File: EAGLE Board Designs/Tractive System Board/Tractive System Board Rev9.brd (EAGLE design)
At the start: 200 x 65 mm, 151 parts, among them K1 RELAY_SPST_NO_D_24, Q2 TRANSISTOR_N_MOS__PMV15ENEA, U1 OPAMP_1_CHANNEL_OPA991, U10 LTC6994-2, U5 RELAY_SOLIDSTATE_NO_AB38S-Q-A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, U6 LT8315, U7 AMC3330_AIRGAP, U8 AMC3330_AIRGAP

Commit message: update
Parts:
- moved D9 61.6 mm to (86.2, 27.4)
- moved D2 46.0 mm to (87.7, 23.3), turned to 270 degrees
- moved R15 45.5 mm to (86.1, 23.5), turned to 90 degrees
- moved R40 44.3 mm to (84.0, 22.8), turned to 270 degrees
- moved R49 43.7 mm to (82.5, 22.8), turned to 90 degrees
- moved C30 43.5 mm to (80.9, 22.7), turned to 270 degrees
- moved R51 42.9 mm to (78.7, 22.1), turned to 0 degrees
- moved D12 42.3 mm to (47.8, 13.2), turned to 90 degrees
- moved C9 40.9 mm to (52.3, 13.4), turned to 270 degrees
- moved C6 40.9 mm to (50.7, 13.4), turned to 270 degrees
- moved R18 40.6 mm to (87.6, 19.8), turned to 90 degrees
- moved C56 40.0 mm to (86.1, 19.7), turned to 270 degrees
- moved L1 39.7 mm to (66.7, 17.0), turned to 180 degrees
- moved C5 39.1 mm to (54.5, 14.3), turned to 270 degrees
- moved C3 38.1 mm to (57.1, 14.2), turned to 270 degrees
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
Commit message: update
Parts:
- moved D12 44.2 mm to (26.2, -25.4), turned to 180 degrees
- moved R15 43.7 mm to (52.4, -4.36), turned to 180 degrees
- moved R40 43.1 mm to (52.1, -6.19), turned to 0 degrees
- moved R49 43.0 mm to (52.1, -7.71), turned to 180 degrees
- moved C30 42.9 mm to (52.2, -9.23), turned to 0 degrees
- moved R51 42.8 mm to (52.8, -12.0), turned to 90 degrees
- moved C3 41.8 mm to (34.3, -20.8)
- moved C5 41.8 mm to (31.6, -20.8)
- moved L1 41.8 mm to (43.8, -18.0)
- moved D2 40.6 mm to (62.9, -8.84), turned to 180 degrees
- moved C6 40.6 mm to (27.9, -20.1)
- moved C9 40.6 mm to (29.5, -20.1)
- moved D11 39.9 mm to (54.5, -16.6), turned to 180 degrees
- moved R18 39.4 mm to (55.9, -3.56), turned to 180 degrees
- moved TS-FUSED 39.0 mm to (69.1, -23.6)
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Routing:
- net TS+FUSED: track 142.7 -> 131.4 mm
- net TS-FUSED: vias 13 -> 12

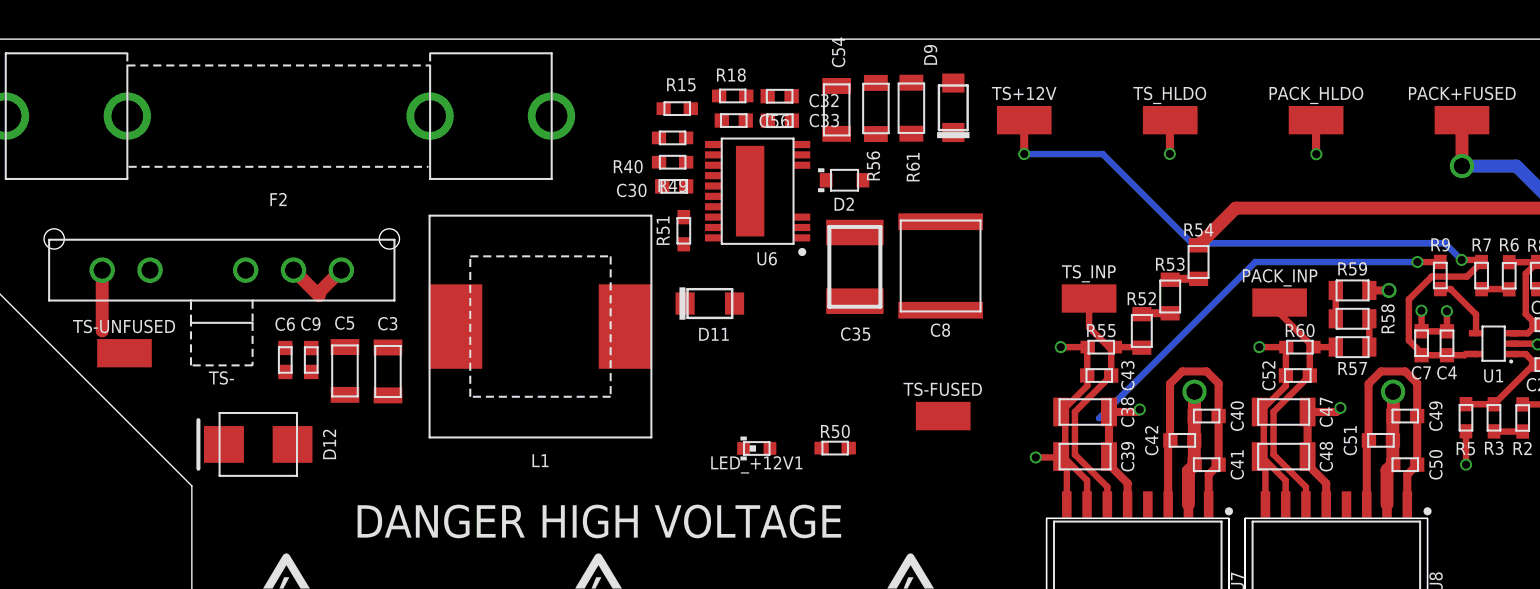
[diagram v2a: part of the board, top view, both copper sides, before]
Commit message: rev9-reroute-first-attempt
modified based on femke's design
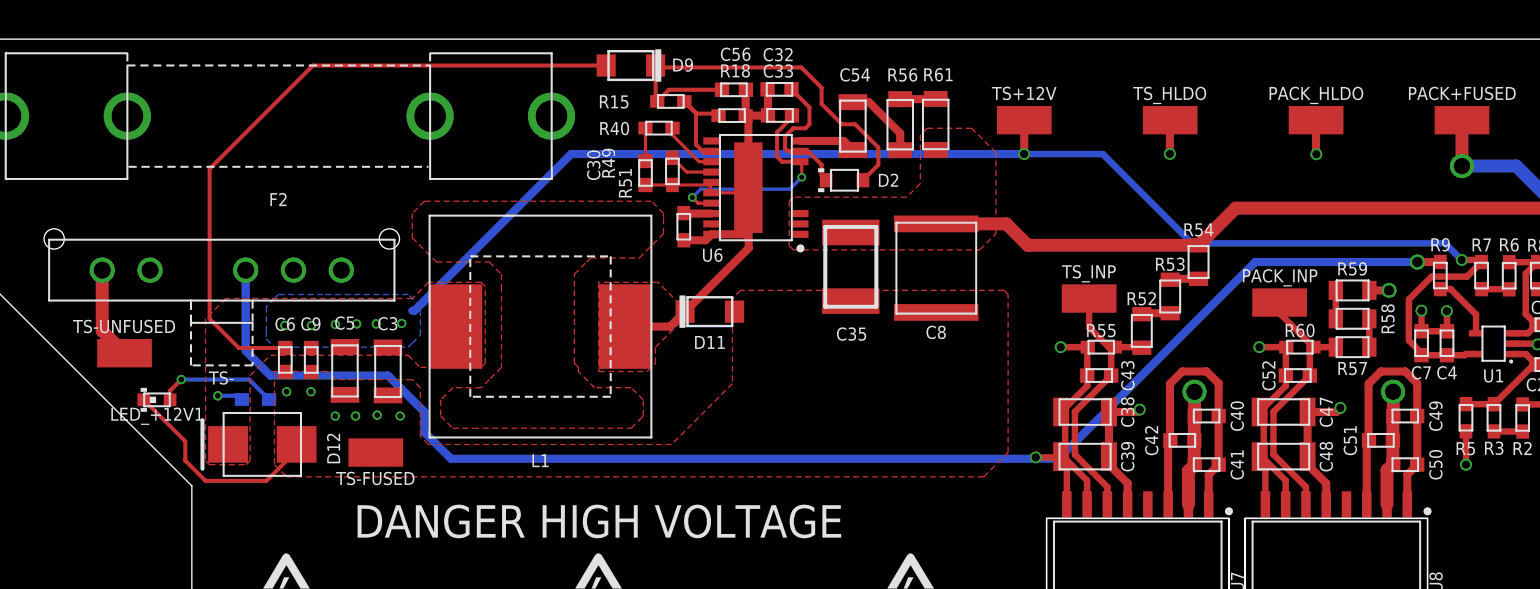
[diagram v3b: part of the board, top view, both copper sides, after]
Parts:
- moved LED_+12V1 37.7 mm to (19.8, -22.6)
- moved R50 36.4 mm to (26.0, -22.6), flipped to the bottom
- moved TS-FUSED 35.6 mm to (33.5, -25.9)
- moved D9 20.4 mm to (49.5, -1.65), turned to 0 degrees
- moved C30 1.99 mm to (50.4, -8.39), turned to 270 degrees
- moved C56 1.93 mm to (56.0, -3.17)
- moved R56 1.83 mm to (66.4, -5.36)
- moved R61 1.83 mm to (68.6, -5.35)
- moved C54 1.44 mm to (63.4, -5.45)
- moved R18 1.23 mm to (55.9, -4.79)
- moved R40 1.05 mm to (51.3, -5.58)
- moved R15 0.60 mm to (52.0, -3.91)
- moved R49 0.57 mm to (52.1, -8.29), turned to 90 degrees
- moved D11 0.51 mm to (54.5, -17.1)
- moved C32 0.43 mm to (58.8, -3.15)
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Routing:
- net TS+12V: track 46.5 -> 132.9 mm, vias 2 -> 9
- net AIL+: track 26.0 -> 88.6 mm
- net PGND: track 0.00 -> 38.4 mm
- net N$1: track 0.00 -> 25.8 mm
- net TS+FUSED: track 131.4 -> 148.4 mm
- net INTVCC: track 0.00 -> 14.3 mm, vias 0 -> 2
- net TS-FUSED: track 65.0 -> 74.1 mm, vias 12 -> 18
- net BIAS: track 0.00 -> 9.05 mm
- net N$44: track 0.00 -> 7.58 mm, vias 0 -> 1
- net FB: track 0.00 -> 6.66 mm
- net N$35: track 0.00 -> 4.84 mm
- net VC: track 0.00 -> 3.58 mm
- net DCM: track 0.00 -> 3.54 mm
- net IREG/SS: track 0.00 -> 2.82 mm
- net N$34: track 0.00 -> 2.23 mm
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- added copper zone on layer 1, net CUTOUT
- added copper zone on layer 1, net PGND
- added copper zone on layer 1, net TS+12V
- added copper zone on layer 16, net TS+12V
- added copper zone on layer 1, net TS+FUSED
- added copper zone on layer 1, net TS-FUSED

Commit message: small update
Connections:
- net PGND renamed SW
- net PACK+FUSED: no longer R4.2
- net TS+FUSED: now also R4.2
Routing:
- net TS+12V: track 132.9 -> 162.3 mm
- net TS+FUSED: track 148.4 -> 164.8 mm
- net AIL+: track 88.6 -> 80.3 mm
- net PACK+FUSED: track 41.7 -> 37.4 mm, vias 3 -> 2
- net SW: track 38.4 -> 34.4 mm
- net N$1: track 25.8 -> 23.3 mm
- net TS-FUSED: vias 18 -> 37

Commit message: updated precharge relay
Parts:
- K1: value RELAY_SPST_NO_D_24 -> RELAY_SPST_NO_D_200W_24
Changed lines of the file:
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@@
 <drawing>
 <settings>
-<setting alwaysvectorfont="no"/>
+<setting alwaysvectorfont="yes"/>
 <setting keepoldvectorfont="yes"/>
 <setting verticaltext="up"/>
@@
 <attribute name="NAME" x="44.704" y="-50.546" size="1.27" layer="25" font="vector" rot="R270" align="bottom-center"/>
 </element>
-<element name="K1" library="HyTechDevices" package="D" value="RELAY_SPST_NO_D_24" x="138.938" y="-46.99" smashed="yes" rot="R180">
-<attribute name="DKPN" value="725-1048-ND" x="95.758" y="-5.08" size="1.778" layer="27" rot="R180" display="off"/>
+<element name="K1" library="HyTechDevices" package="D" value="RELAY_SPST_NO_D_200W_24" x="138.938" y="-46.99" smashed="yes" rot="R180">
+<attribute name="DKPN" value="725-1362-ND" x="95.758" y="-5.08" size="1.778" layer="27" rot="R180" display="off"/>
 <attribute name="MANUFACTURER" value="Sensata-Cynergy3" x="95.758" y="-5.08" size="1.778" layer="27" rot="R180" display="off"/>
-<attribute name="MOPN" value="285-DAR72410" x="95.758" y="-5.08" size="1.778" layer="27" rot="R180" display="off"/>
-<attribute name="MPN" value="DAR72410" x="95.758" y="-5.08" size="1.778" layer="27" rot="R180" display="off"/>
+<attribute name="MOPN" value="285-DAT200-24" x="95.758" y="-5.08" size="1.778" layer="27" rot="R180" display="off"/>
+<attribute name="MPN" value="DAT200-24" x="95.758" y="-5.08" size="1.778" layer="27" rot="R180" display="off"/>
 <attribute name="NAME" x="169.9" y="-47.018" size="0.8128" layer="21" font="vector" rot="R270" align="bottom-center"/>
 </element>
@@
 <vertex x="55.88" y="-21.59"/>
 <vertex x="52.07" y="-25.4"/>
-<vertex x="36.83" y="-25.4"/>
-<vertex x="36.322" y="-24.892"/>
+<vertex x="36.576" y="-25.4"/>
+<vertex x="36.322" y="-25.146"/>
 <vertex x="36.322" y="-21.844"/>
 <vertex x="35.814" y="-21.336"/>

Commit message: sch changes from testing
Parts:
- removed C56: CAPACITOR_0603_50V_10NF, HyTechDevices:0603-CAP
- removed R49: RESISTOR_0603_5.9K, HyTechDevices:0603-RES
- added C10: CAPACITOR_0603_50V_0.1UF, HyTechDevices:0603-CAP
- added D1: RECTIFIER_800V_SOD-123FA, HyTechDevices:SOD-123FA
- added R1: RESISTOR_0603_DNP, HyTechDevices:0603-RES
- R30: value RESISTOR_0603_3.3K -> RESISTOR_0603_12K
- R42: value RESISTOR_0603_DNP -> RESISTOR_0603_12K
- moved TS+12V 5.08 mm to (79.2, -5.08)
- moved TS_HLDO 3.56 mm to (86.9, -5.08)
- moved PACK_HLDO 2.54 mm to (95.0, -5.08)
- moved PACK+FUSED 1.27 mm to (102.9, -5.08)
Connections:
- new net DRAIN: C35.1, C8.1, D1.C, R61.1, U6.1, U6.2, U6.3
- new net N$4: R1.2
- net IREG/SS: now also C10.1; no longer R49.2
- net N$1: no longer C56.1
- net SW: now also C10.2; no longer C56.2, R49.1
- net TS+12V: now also R1.1
- net TS+FUSED: now also D1.A; no longer C35.1, C8.1, R54.2, R61.1, U6.1, U6.2, U6.3
- net TS+UNFUSED: now also R54.2
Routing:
- net TS+FUSED: track 164.8 -> 156.0 mm
- net SW: track 34.4 -> 30.5 mm
- net TS_HLDO_OUT: track 27.2 -> 28.7 mm
- net N$1: track 23.3 -> 21.9 mm
- net IREG/SS: track 2.82 -> 1.56 mm
- net PACK+FUSED: track 37.4 -> 36.3 mm

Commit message: some more routing
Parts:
- added J1: CONNECTOR-2_μF_T_V_BLACK, HyTechDevices:MOLEX_MICROFIT_PTH_VERTICAL_02_DUAL
- moved D1 97.4 mm to (76.2, -10.7), turned to 180 degrees
- moved C10 85.2 mm to (52.1, -8.38), turned to 270 degrees
- moved R1 67.5 mm to (26.4, -7.62), flipped to the bottom, turned to 180 degrees
- moved TS+ 6.37 mm to (191.0, -42.9)
- moved R54 2.90 mm to (82.3, -14.7), turned to 0 degrees
- moved R53 1.13 mm to (82.3, -16.6), turned to 180 degrees
- moved R52 0.80 mm to (82.3, -18.5), turned to 0 degrees
- moved R9 0.77 mm to (100.2, -15.6), flipped to the bottom, turned to 180 degrees
- moved R4 0.25 mm to (107.3, -24.0)
- turned R5 to 270 degrees
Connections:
- removed net N$4: R1.2
- net AIL+: now also J1.1, R1.2
- net TS-FUSED: now also J1.2
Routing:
- net AIL+: track 80.3 -> 271.5 mm, vias 1 -> 0
- net TS-FUSED: track 74.1 -> 193.3 mm, vias 37 -> 38
- net TS+UNFUSED: track 103.5 -> 149.2 mm, vias 0 -> 1
- net IT-: track 72.0 -> 52.7 mm
- net IT+: track 73.1 -> 53.8 mm
- net TS+FUSED: track 156.0 -> 163.5 mm
- net DRAIN: track 0.00 -> 6.37 mm
- net PACK+: track 133.9 -> 139.1 mm
- net SHDN: track 182.4 -> 178.6 mm
- net SW: track 30.5 -> 33.0 mm
- net TS+12V: track 162.3 -> 164.8 mm
- net TS_HLDO_OUT: track 28.7 -> 30.6 mm
- net TS_INP: track 17.4 -> 15.7 mm
- net N$3: track 85.1 -> 83.5 mm
- net IREG/SS: track 1.56 -> 2.83 mm
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- added copper zone on layer 1, net DRAIN
- removed copper zone on layer 1, net TS+FUSED

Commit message: some more routing
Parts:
- moved TS+ 0.57 mm to (190.5, -42.7)
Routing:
- net TS_INP: track 15.7 -> 17.4 mm
- net TS+UNFUSED: track 149.2 -> 148.5 mm
- net TS+FUSED: track 163.5 -> 162.9 mm
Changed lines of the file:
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@@
 <attribute name="NAME" x="23.876" y="-20.828" size="0.8128" layer="25" rot="R180" align="bottom-center"/>
 </element>
-<element name="TS+" library="HyTechDevices" package="MOLEX_MICROFIT_PTH_VERTICAL_07_SINGLE_SPACED" value="CONNECTOR-5_MICRO_V7S_" x="191.008" y="-42.926" smashed="yes" rot="R270">
-<attribute name="MANUFACTURER" value="Molex" x="74.168" y="-69.596" size="1.778" layer="27" rot="R270" display="off"/>
-<attribute name="MPN" value="43650-0717" x="74.168" y="-69.596" size="1.778" layer="27" rot="R270" display="off"/>
-<attribute name="NAME" x="197.358" y="-42.926" size="0.8128" layer="25" rot="R270" align="bottom-center"/>
+<element name="TS+" library="HyTechDevices" package="MOLEX_MICROFIT_PTH_VERTICAL_07_SINGLE_SPACED" value="CONNECTOR-5_MICRO_V7S_" x="190.5" y="-42.672" smashed="yes" rot="R270">
+<attribute name="MANUFACTURER" value="Molex" x="73.66" y="-69.342" size="1.778" layer="27" rot="R270" display="off"/>
+<attribute name="MPN" value="43650-0717" x="73.66" y="-69.342" size="1.778" layer="27" rot="R270" display="off"/>
+<attribute name="NAME" x="196.85" y="-42.672" size="0.8128" layer="25" rot="R270" align="bottom-center"/>
 </element>
 <element name="ACU" library="HyTechDevices" package="MOLEX_MICROFIT_PTH_VERTICAL_08_DUAL" value="CONNECTOR-8_μF_T_V_BLACK" x="38.354" y="-50.546" smashed="yes" rot="R270">
@@
 <wire x1="140.97" y1="-20.574" x2="133.096" y2="-20.574" width="0.8128" layer="1"/>
 <wire x1="133.096" y1="-20.574" x2="123.1138" y2="-10.5918" width="0.8128" layer="1"/>
-<wire x1="190.8556" y1="-46.0756" x2="176.53" y2="-46.0756" width="0.8128" layer="1"/>
-<wire x1="190.8556" y1="-46.0756" x2="191.008" y2="-45.9232" width="0.8128" layer="1"/>
+<wire x1="190.0936" y1="-46.0756" x2="176.53" y2="-46.0756" width="0.8128" layer="1"/>
+<wire x1="190.0936" y1="-46.0756" x2="190.5" y2="-45.6692" width="0.8128" layer="1"/>
 <contactref element="R4" pad="2"/>
 <contactref element="D1" pad="A"/>
-<wire x1="107.356421875" y1="-25.129978125" x2="107.2642" y2="-25.03775625" width="0.508" layer="1"/>
-<wire x1="107.2642" y1="-25.03775625" x2="128.63224375" y2="-25.03775625" width="0.508" layer="1"/>
-<wire x1="128.63224375" y1="-25.03775625" x2="133.096" y2="-20.574" width="0.508" layer="1"/>
+<wire x1="133.096" y1="-20.574" x2="128.63224375" y2="-25.03775625" width="0.508" layer="1"/>
 <wire x1="77.8262" y1="-10.5918" x2="77.75" y2="-10.668" width="0.8128" layer="1"/>
 <wire x1="123.1138" y1="-10.5918" x2="77.8262" y2="-10.5918" width="0.8128" layer="1"/>
+<wire x1="128.63224375" y1="-25.03775625" x2="107.2642" y2="-25.03775625" width="0.508" layer="1"/>
 </signal>
 <signal name="TS_INP">
@@
 <wire x1="79.460975" y1="-19.304" x2="78.232" y2="-18.075025" width="0.4064" layer="1"/>
 <wire x1="78.232" y1="-16.256" x2="78.232" y2="-18.075025" width="0.4064" layer="1"/>
-<wire x1="79.844" y1="-19.304" x2="81.246" y2="-18.542" width="0" layer="19" extent="1-1"/>
+<wire x1="81.246" y1="-18.542" x2="80.484" y2="-19.304" width="0.4064" layer="1"/>
+<wire x1="80.484" y1="-19.304" x2="79.844" y2="-19.304" width="0.4064" layer="1"/>
 </signal>
 <signal name="TS+12V">
@@
 <via x="27.94" y="-22.098" extent="1-16" drill="0.35"/>
 <via x="29.464" y="-22.098" extent="1-16" drill="0.35"/>
-<via x="30.988" y="-23.622" extent="1-16" drill="0.35"/>
+<via x="30.9499" y="-23.6347" extent="1-16" drill="0.35"/>
 <via x="32.258" y="-23.622" extent="1-16" drill="0.35"/>
-<via x="33.6169" y="-23.568659375" extent="1-16" drill="0.35"/>
+<via x="33.5762625" y="-23.632159375" extent="1-16" drill="0.35"/>
 <via x="35.052" y="-23.622" extent="1-16" drill="0.35"/>
 <wire x1="18.987" y1="-22.606" x2="21.59" y2="-25.209" width="0.254" layer="1"/>
@@
 <wire x1="116.078" y1="-18.034" x2="116.078" y2="-31.242" width="0.8128" layer="15"/>
 <wire x1="169.7609" y1="-12.7" x2="121.412" y2="-12.7" width="0.8128" layer="15"/>
-<wire x1="191.008" y1="-33.9344" x2="191.008" y2="-36.9316" width="0.8128" layer="15"/>
-<wire x1="191.008" y1="-33.9344" x2="188.468" y2="-31.3944" width="0.8128" layer="15"/>
-<wire x1="188.468" y1="-31.3944" x2="180.8226" y2="-31.3944" width="0.8128" layer="15"/>
-<wire x1="180.8226" y1="-31.3944" x2="176.53" y2="-27.1018" width="0.8128" layer="15"/>
+<wire x1="190.5" y1="-33.6804" x2="190.5" y2="-36.6776" width="0.8128" layer="15"/>
+<wire x1="190.5" y1="-33.6804" x2="189.23" y2="-32.4104" width="0.8128" layer="15"/>
+<wire x1="189.23" y1="-32.4104" x2="181.8386" y2="-32.4104" width="0.8128" layer="15"/>
+<wire x1="181.8386" y1="-32.4104" x2="176.53" y2="-27.1018" width="0.8128" layer="15"/>
 <contactref element="R54" pad="2"/>
 <wire x1="108.712" y1="-31.242" x2="103.632" y2="-26.162" width="0.508" layer="15"/>
@@
 <contactref element="K1" pad="2"/>
 <contactref element="PACK+" pad="1"/>
-<wire x1="191.008" y1="-51.9176" x2="191.008" y2="-48.514" width="0.8128" layer="2"/>
-<wire x1="191.008" y1="-48.514" x2="182.118" y2="-39.624" width="0.8128" layer="2"/>
+<wire x1="190.5" y1="-51.6636" x2="190.5" y2="-48.006" width="0.8128" layer="2"/>
+<wire x1="190.5" y1="-48.006" x2="182.118" y2="-39.624" width="0.8128" layer="2"/>
 <wire x1="182.118" y1="-39.624" x2="164.846" y2="-39.624" width="0.8128" layer="2"/>
 <wire x1="164.846" y1="-39.624" x2="149.86" y2="-24.638" width="0.8128" layer="2"/>
@@
 <contactref element="R3" pad="1"/>
 <contactref element="R5" pad="2"/>
-<wire x1="103.60405625" y1="-22.8837625" x2="103.598975" y2="-22.87868125" width="0.4064" layer="1"/>
 <wire x1="104.681196875" y1="-19.73555625" x2="105.59194375" y2="-19.73555625" width="0.4064" layer="1"/>
 <wire x1="105.59194375" y1="-19.73555625" x2="106.255125" y2="-20.3987375" width="0.4064" layer="1"/>
@@
 <contactref element="C33" pad="2"/>
 <wire x1="58.109415625" y1="-3.18006875" x2="58.078946875" y2="-3.1496" width="0.4064" layer="1"/>
-<wire x1="54.416659375" y1="-9.138025" x2="54.51034375" y2="-9.044340625" width="0.2032" layer="1"/>
 <wire x1="54.51034375" y1="-9.044340625" x2="54.573121875" y2="-8.9815625" width="0.2032" layer="1"/>
 <wire x1="54.573121875" y1="-9.6315625" x2="54.51034375" y2="-9.568784375" width="0.2032" layer="1"/>
@@
 <wire x1="52.8294625" y1="-12.605121875" x2="54.1995625" y2="-12.605121875" width="0.508" layer="1"/>
 <wire x1="54.1995625" y1="-12.605121875" x2="54.573121875" y2="-12.2315625" width="0.508" layer="1"/>
-<wire x1="52.91268125" y1="-17.078959375" x2="51.977959375" y2="-18.01368125" width="0.508" layer="1"/>
-<wire x1="51.977959375" y1="-18.01368125" x2="49.17301875" y2="-18.01368125" width="0.508" layer="1"/>
+<wire x1="52.91268125" y1="-17.078959375" x2="51.977959375" y2="-18.01368125" width="0.6096" layer="1"/>
+<wire x1="51.977959375" y1="-18.01368125" x2="49.17301875" y2="-18.01368125" width="0.6096" layer="1"/>
 <polygon width="0.2032" layer="1" thermals="no">
 <vertex x="52.578" y="-16.629378125"/>
@@
 <wire x1="58.10179375" y1="-4.790440625" x2="58.109415625" y2="-4.78281875" width="0.508" layer="1"/>
 <wire x1="58.109415625" y1="-4.78281875" x2="58.109415625" y2="-3.18006875" width="0.508" layer="1"/>
-<wire x1="52.91268125" y1="-17.078959375" x2="56.878121875" y2="-13.11351875" width="0.508" layer="1"/>
-<wire x1="56.878121875" y1="-12.2315625" x2="56.878121875" y2="-13.11351875" width="0.508" layer="1"/>
+<wire x1="52.91268125" y1="-17.078959375" x2="56.878121875" y2="-13.11351875" width="0.6096" layer="1"/>
+<wire x1="56.878121875" y1="-12.2315625" x2="56.878121875" y2="-13.11351875" width="0.6096" layer="1"/>
 <wire x1="56.878121875" y1="-9.3065625" x2="56.878121875" y2="-9.611125" width="0.508" layer="1"/>
 <wire x1="56.878121875" y1="-9.611125" x2="56.857684375" y2="-9.6315625" width="0.508" layer="1"/>
